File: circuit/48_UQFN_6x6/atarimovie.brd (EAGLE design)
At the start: 72.4 x 82.5 mm, 24 parts, among them IC1 AMS1117-3.3V, J1 CARTRIDGE EDGE, J2 TF-15X15, U1 DSPIC33CKXXMC105-X_M4, U2 74LVCH245APW,118, U3 74LVCH245APW,118, X1 22-23-2051

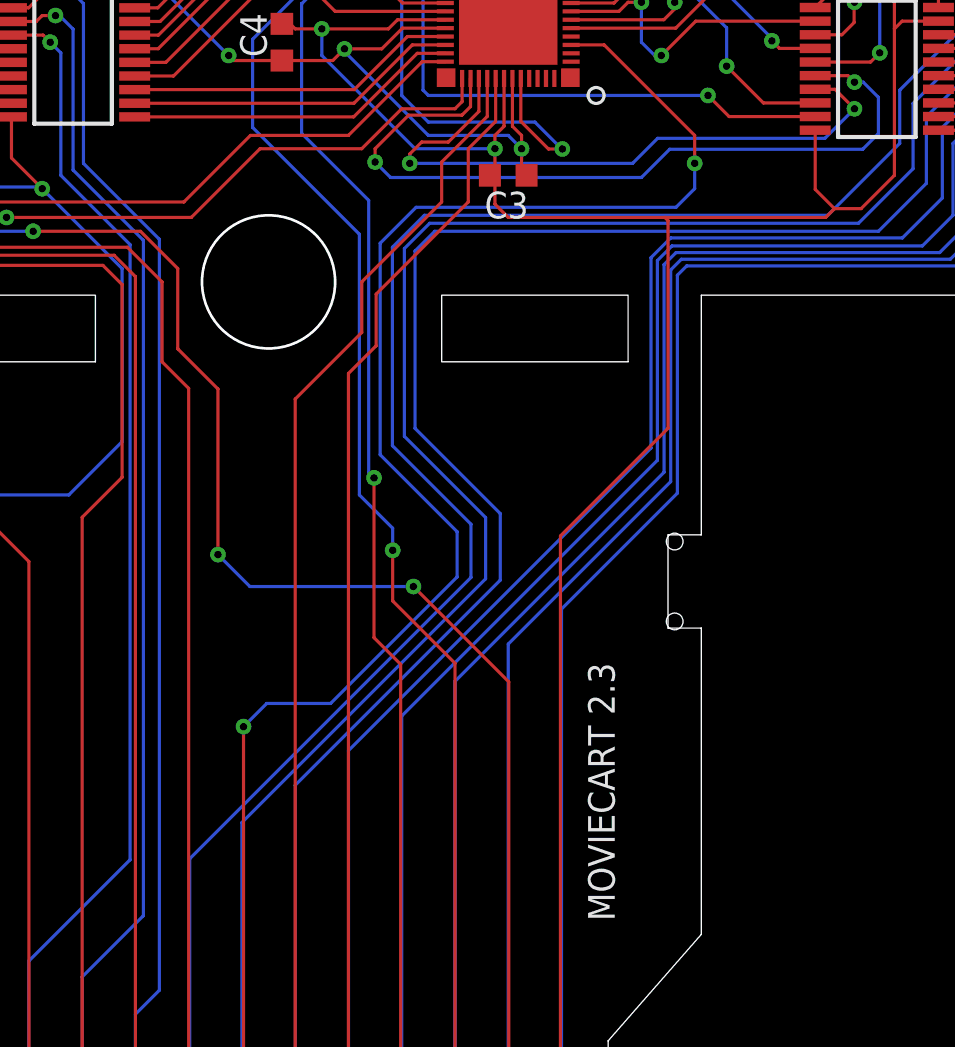
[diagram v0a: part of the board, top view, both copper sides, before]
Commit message: PCB: slightly widened post hole from 3.175 to 3.210 mm
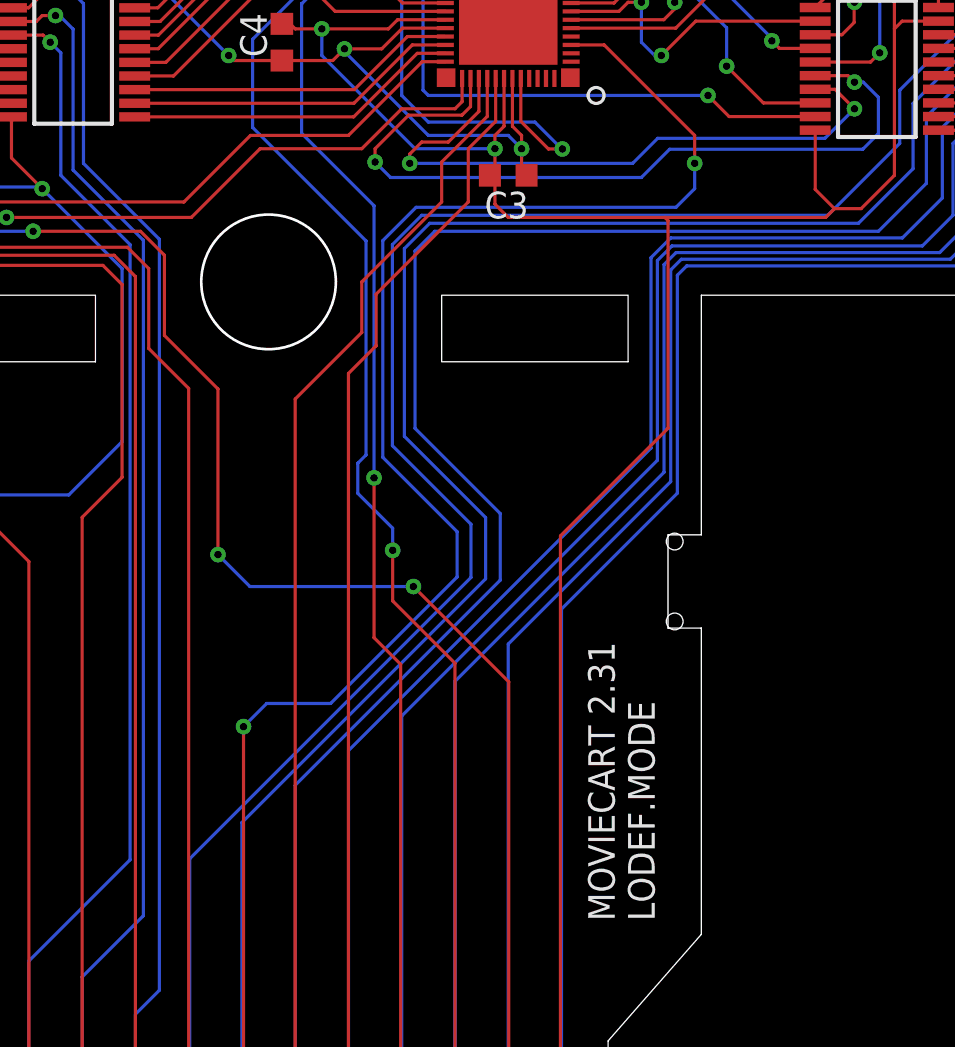
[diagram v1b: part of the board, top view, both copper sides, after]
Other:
- board text added: "LODEF.MODE"
- board text added: "MOVIECART 2.31"
- board text removed: "MOVIECART 2.3"
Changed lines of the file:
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@@
 <board>
 <plain>
-<text x="53.34" y="20.955" size="1.27" layer="21" font="vector" rot="R90">MOVIECART 2.3</text>
+<text x="53.34" y="20.955" size="1.27" layer="21" font="vector" rot="R90">MOVIECART 2.31</text>
 <text x="14.6685" y="76.835" size="1.016" layer="21" rot="R270">VPP</text>
 <text x="12.065" y="76.835" size="1.016" layer="21" rot="R270">VDD</text>
@@
 <text x="56.0705" y="75.2475" size="1.016" layer="25">SDCS</text>
 <text x="19.1135" y="59.944" size="1.016" layer="25">SDO</text>
+<text x="55.245" y="20.955" size="1.27" layer="21" font="vector" rot="R90">LODEF.MODE</text>
 </plain>
 <attributes>
@@
 <wire x1="71.12" y1="64.73915" x2="71.12" y2="64.77" width="0.1524" layer="1"/>
 <wire x1="69.59924375" y1="63.21839375" x2="71.12" y2="64.73915" width="0.1524" layer="1"/>
-<wire x1="42.7355" y1="43.6245" x2="42.7355" y2="53.086" width="0.1524" layer="16"/>
-<wire x1="42.7355" y1="53.086" x2="44.2595" y2="54.61" width="0.1524" layer="16"/>
-<wire x1="63.5" y1="54.61" x2="44.2595" y2="54.61" width="0.1524" layer="16"/>
+<wire x1="42.7355" y1="43.6245" x2="42.7355" y2="53.213" width="0.1524" layer="16"/>
+<wire x1="42.7355" y1="53.213" x2="44.1325" y2="54.61" width="0.1524" layer="16"/>
+<wire x1="63.5" y1="54.61" x2="44.1325" y2="54.61" width="0.1524" layer="16"/>
 <wire x1="66.929" y1="58.039" x2="63.5" y2="54.61" width="0.1524" layer="16"/>
 <wire x1="46.482" y1="37.338" x2="46.482" y2="39.878" width="0.1524" layer="16"/>
@@
 <wire x1="36.068" y1="58.801" x2="36.068" y2="63.0047" width="0.1524" layer="16"/>
 <wire x1="39.1033" y1="66.04" x2="36.068" y2="63.0047" width="0.1524" layer="16"/>
-<wire x1="41.1607" y1="41.275" x2="41.1607" y2="53.7083" width="0.1524" layer="16"/>
-<wire x1="41.1607" y1="53.7083" x2="36.068" y2="58.801" width="0.1524" layer="16"/>
-<wire x1="42.7482" y1="38.6334" x2="42.7482" y2="39.6875" width="0.1524" layer="16"/>
-<wire x1="42.7482" y1="39.6875" x2="41.1607" y2="41.275" width="0.1524" layer="16"/>
+<wire x1="41.4782" y1="53.3908" x2="41.4782" y2="43.18" width="0.1524" layer="16"/>
+<wire x1="41.4782" y1="53.3908" x2="36.068" y2="58.801" width="0.1524" layer="16"/>
+<wire x1="42.7482" y1="39.6875" x2="42.7482" y2="38.6334" width="0.1524" layer="16"/>
+<wire x1="41.4782" y1="43.18" x2="41.0845" y2="42.7863" width="0.1524" layer="16"/>
+<wire x1="41.0845" y1="42.7863" x2="41.0845" y2="41.3512" width="0.1524" layer="16"/>
+<wire x1="41.0845" y1="41.3512" x2="42.7482" y2="39.6875" width="0.1524" layer="16"/>
 </signal>
 <signal name="CADDR9">
@@
 <wire x1="43.18" y1="3.81" x2="43.1292" y2="3.81" width="0.1524" layer="1"/>
 <via x="41.8592" y="42.0878" extent="1-16" drill="0.35"/>
-<wire x1="41.6052" y1="55.3212" x2="41.6052" y2="42.3418" width="0.1524" layer="16"/>
-<wire x1="41.8592" y1="42.0878" x2="41.6052" y2="42.3418" width="0.1524" layer="16"/>
-<wire x1="41.6052" y1="55.3212" x2="38.4048" y2="58.5216" width="0.1524" layer="16"/>
+<wire x1="41.8592" y1="55.0672" x2="41.8592" y2="42.0878" width="0.1524" layer="16"/>
+<wire x1="41.8592" y1="55.0672" x2="38.4048" y2="58.5216" width="0.1524" layer="16"/>
 <wire x1="43.1292" y1="33.1978" x2="41.8592" y2="34.4678" width="0.1524" layer="1"/>
 <wire x1="41.8592" y1="34.4678" x2="41.8592" y2="42.0878" width="0.1524" layer="1"/>
@@
 <wire x1="57.15" y1="58.42" x2="57.15" y2="57.0865" width="0.1524" layer="1"/>
 <wire x1="57.15" y1="58.42" x2="52.835" y2="62.735" width="0.1524" layer="1"/>
-<wire x1="42.1513" y1="43.1927" x2="42.1513" y2="53.2765" width="0.1524" layer="16"/>
-<wire x1="42.1513" y1="53.2765" x2="43.8658" y2="54.991" width="0.1524" layer="16"/>
+<wire x1="42.2783" y1="43.0657" x2="42.2783" y2="53.4035" width="0.1524" layer="16"/>
+<wire x1="42.2783" y1="53.4035" x2="43.8658" y2="54.991" width="0.1524" layer="16"/>
 <wire x1="56.261" y1="54.991" x2="57.15" y2="55.88" width="0.1524" layer="16"/>
 <wire x1="43.8658" y1="54.991" x2="56.261" y2="54.991" width="0.1524" layer="16"/>
 <wire x1="39.789471875" y1="31.330528125" x2="45.821971875" y2="37.363028125" width="0.1524" layer="16"/>
 <wire x1="45.821971875" y1="37.363028125" x2="45.821971875" y2="39.522028125" width="0.1524" layer="16"/>
-<wire x1="45.821971875" y1="39.522028125" x2="42.1513" y2="43.1927" width="0.1524" layer="16"/>
+<wire x1="45.821971875" y1="39.522028125" x2="42.2783" y2="43.0657" width="0.1524" layer="16"/>
 <wire x1="35.6362" y1="30.226" x2="36.740728125" y2="31.330528125" width="0.1524" layer="16"/>
 <wire x1="39.789471875" y1="31.330528125" x2="36.740728125" y2="31.330528125" width="0.1524" layer="16"/>
@@
 <wire x1="22.352" y1="54.356" x2="23.622" y2="53.086" width="0.1524" layer="1"/>
 <wire x1="23.622" y1="53.086" x2="30.099" y2="53.086" width="0.1524" layer="1"/>
-<wire x1="30.099" y1="53.086" x2="31.75" y2="51.435" width="0.1524" layer="1"/>
-<wire x1="31.75" y1="47.625" x2="33.02" y2="46.355" width="0.1524" layer="1"/>
-<wire x1="31.75" y1="51.435" x2="31.75" y2="47.625" width="0.1524" layer="1"/>
+<wire x1="30.099" y1="53.086" x2="31.115" y2="52.07" width="0.1524" layer="1"/>
+<wire x1="31.115" y1="48.26" x2="33.02" y2="46.355" width="0.1524" layer="1"/>
+<wire x1="31.115" y1="52.07" x2="31.115" y2="48.26" width="0.1524" layer="1"/>
 <wire x1="33.02" y1="46.355" x2="33.02" y2="3.81" width="0.1524" layer="1"/>
 <wire x1="24.5702" y1="59.95339375" x2="23.12339375" y2="59.95339375" width="0.1524" layer="1"/>
@@
 <via x="43.7388" y="36.9062" extent="1-16" drill="0.35"/>
 <wire x1="25.6032" y1="53.848" x2="30.7213" y2="53.848" width="0.1524" layer="1"/>
-<wire x1="30.7213" y1="53.848" x2="32.4993" y2="52.07" width="0.1524" layer="1"/>
-<wire x1="32.4993" y1="52.07" x2="32.4993" y2="48.2441625" width="0.1524" layer="1"/>
-<wire x1="32.4993" y1="48.2441625" x2="34.417" y2="46.3264625" width="0.1524" layer="1"/>
+<wire x1="30.7213" y1="53.848" x2="31.8643" y2="52.705" width="0.1524" layer="1"/>
+<wire x1="31.8643" y1="52.705" x2="31.8643" y2="48.8791625" width="0.1524" layer="1"/>
+<wire x1="31.8643" y1="48.8791625" x2="34.417" y2="46.3264625" width="0.1524" layer="1"/>
 <wire x1="34.417" y1="46.3264625" x2="34.417" y2="38.4302" width="0.1524" layer="1"/>
 <contactref element="IC1" pad="3"/>
